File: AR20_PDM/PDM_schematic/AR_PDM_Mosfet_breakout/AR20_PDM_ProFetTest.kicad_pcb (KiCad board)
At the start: 2 copper layers, 26.7 x 27.9 mm, 4 parts, among them J1 Conn_01x05_Female, Q1 BTS50025-1TAD

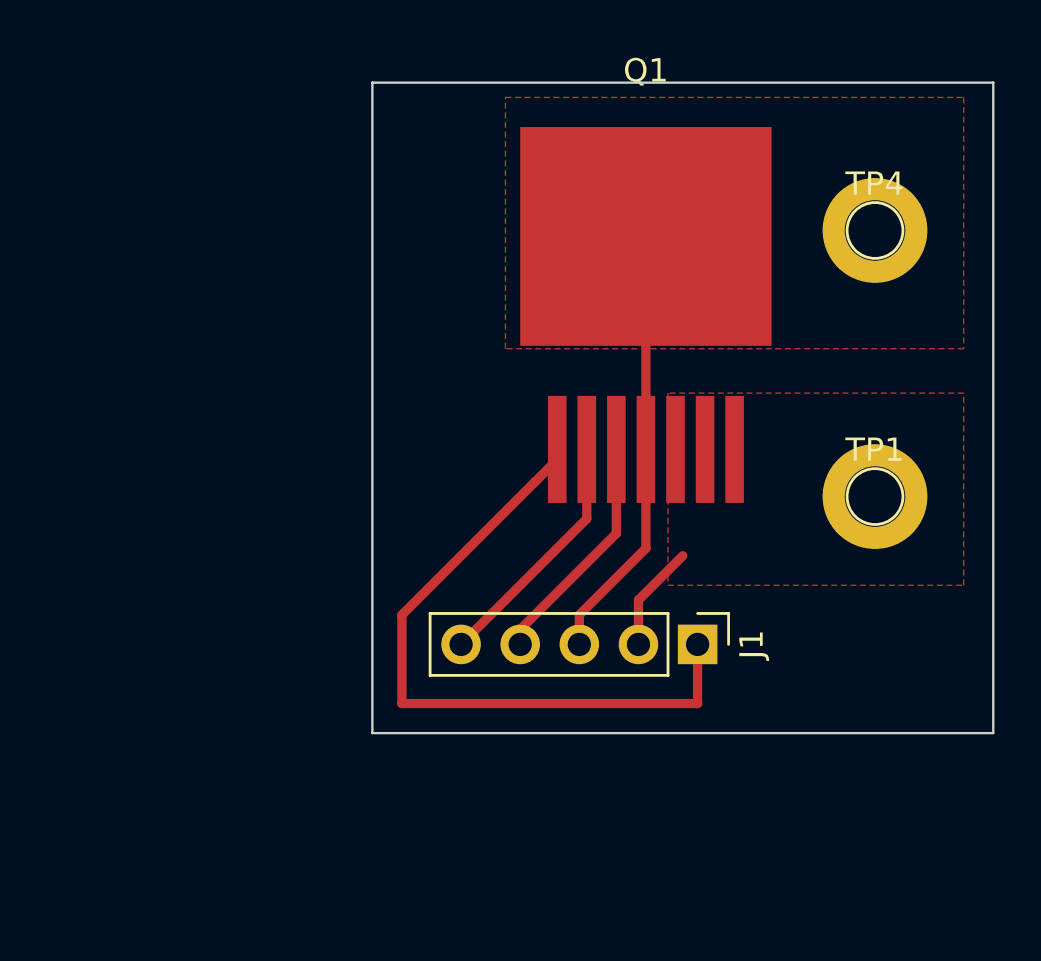
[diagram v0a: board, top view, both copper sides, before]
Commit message: Revert "Merge branch 'master' into GPS"
This reverts commit eede9093351da36afd50b96e1e304890f671bac6.
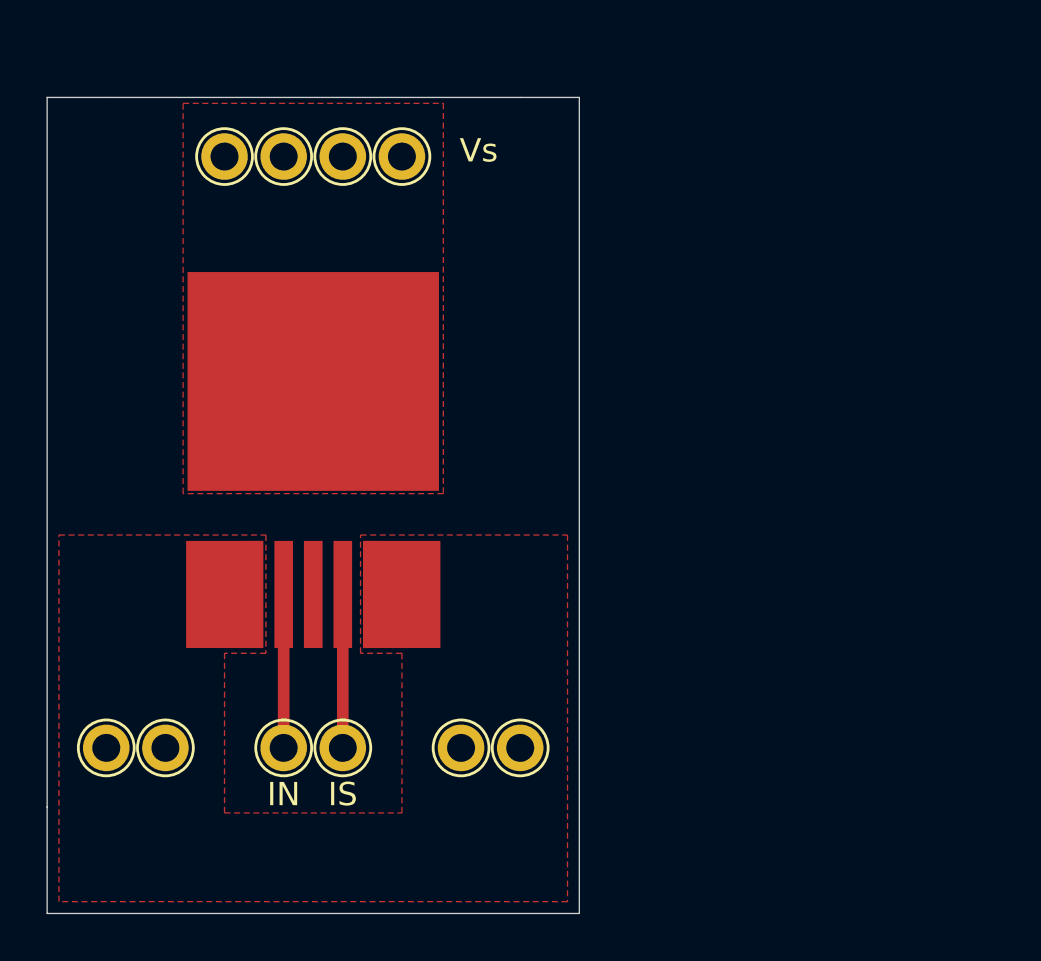
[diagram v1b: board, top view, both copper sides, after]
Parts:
- removed J1: Conn_01x05_Female, Connector_PinHeader_2.54mm:PinHeader_1x05_P2.54mm_Vertical
- removed Q1: BTS50025-1TAD, AR_Footprints:BTS500xx
- removed TP1, TP4: TestPoint, AR_Footprints:Supp_THT_Hole
- added ?: BTS50055-1TMA, PDM_footprint:BTS50055-1TMA, F.Cu at (123.2, 102.9)
- added ?: , PDM_footprint:THT_hole_2.2mm_1.2mm, F.Cu at (129.5, 111.8)
- added ?: , PDM_footprint:THT_hole_2.2mm_1.2mm, F.Cu at (132.1, 111.8)
- added ?: , PDM_footprint:THT_hole_2.2mm_1.2mm, F.Cu at (116.8, 111.8)
- added ?: , PDM_footprint:THT_hole_2.2mm_1.2mm, F.Cu at (114.3, 111.8)
- added ?: , PDM_footprint:THT_hole_2.2mm_1.2mm, F.Cu at (119.4, 86.4)
- added ?: , PDM_footprint:THT_hole_2.2mm_1.2mm, F.Cu at (121.9, 86.4)
- added ?: , PDM_footprint:THT_hole_2.2mm_1.2mm, F.Cu at (124.5, 86.4)
- added ?: , PDM_footprint:THT_hole_2.2mm_1.2mm, F.Cu at (127.0, 86.4)
- added IN: , TestPoint:TestPoint_THTPad_D2.0mm_Drill1.0mm, F.Cu at (121.9, 111.8)
- added IS: , TestPoint:TestPoint_THTPad_D2.0mm_Drill1.0mm, F.Cu at (124.5, 111.8)
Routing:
- net GND: track 28.9 -> 0.00 mm
- net VS: track 18.7 -> 0.00 mm
- net (no net): track 0.00 -> 13.2 mm
- net IN: track 10.6 -> 0.00 mm
- net IS: track 10.1 -> 0.00 mm
- net OUT: track 4.60 -> 0.00 mm
- added copper zone on F.Cu, net (none)
- removed copper zone on F.Cu, net OUT
- removed copper zone on F.Cu, net VS
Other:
- board size 26.7 x 27.9 mm -> 22.9 x 35.1 mm
- rule pad_to_mask_clearance: 0 -> 0.051
- board text added: "Vs"
